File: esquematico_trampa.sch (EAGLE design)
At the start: 17 parts, among them U1 MICROCHIP_MCP3008-I-PMICROCHI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, U2 LM358PE3

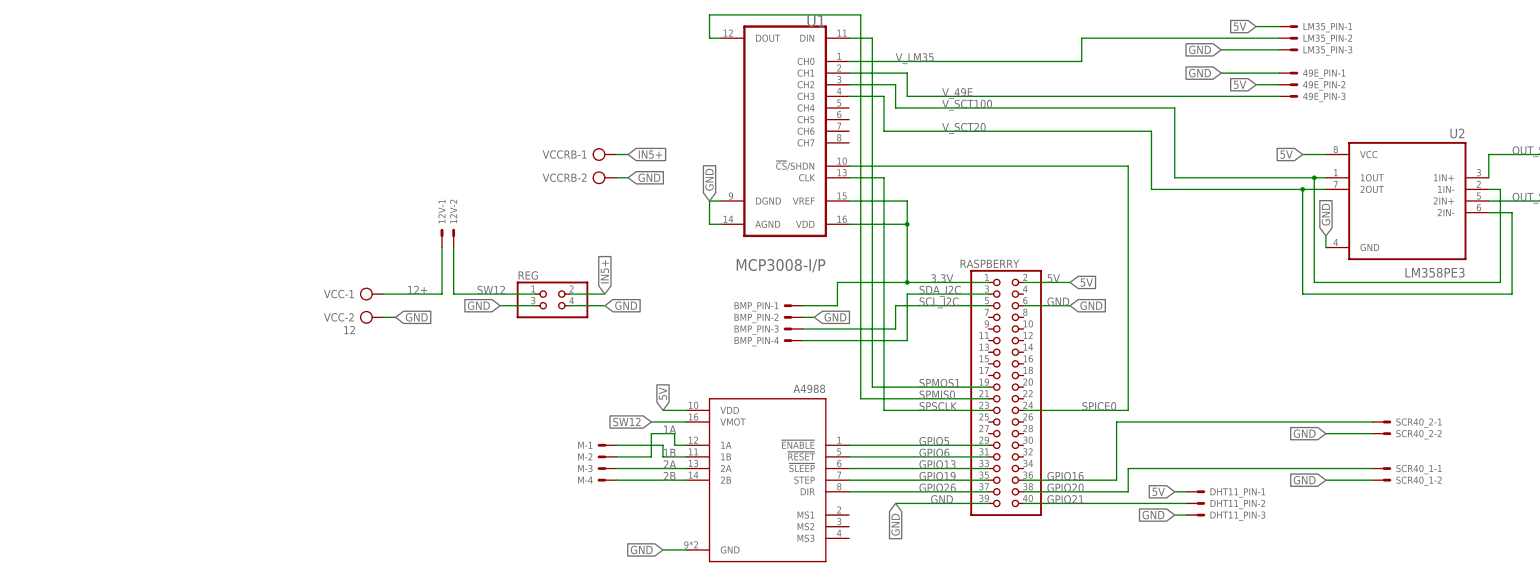
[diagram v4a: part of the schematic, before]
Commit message: esquematico con cambios en gpio7
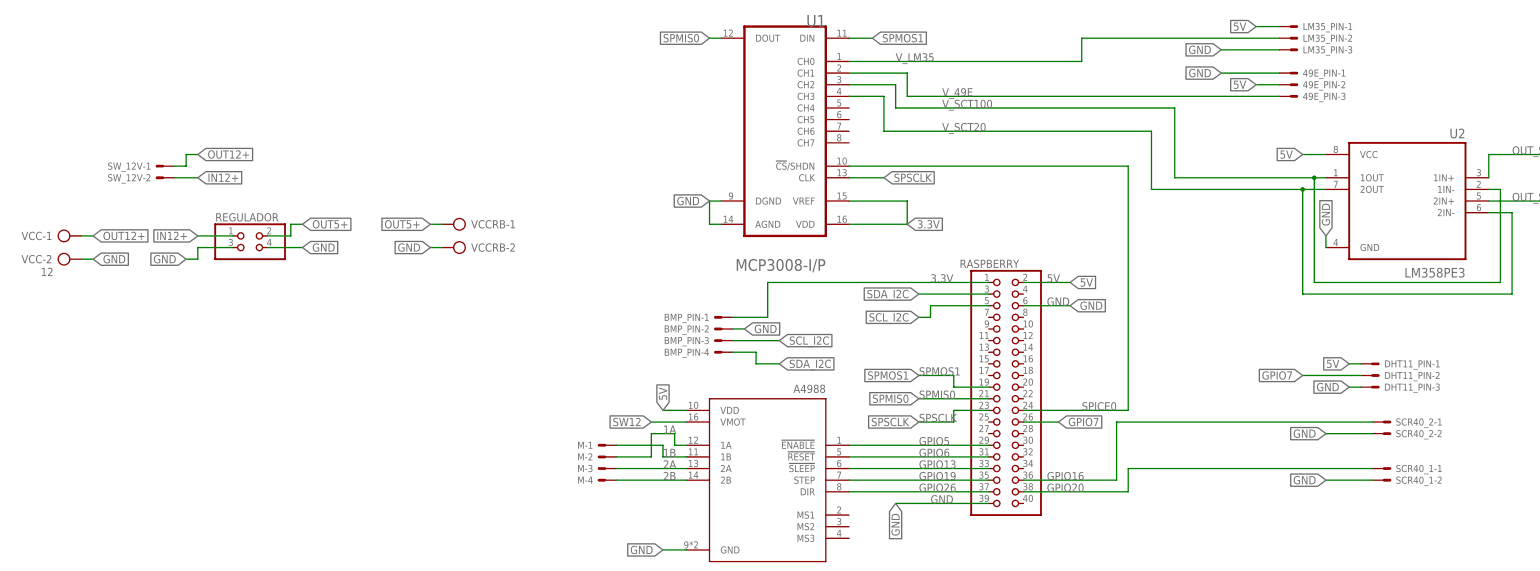
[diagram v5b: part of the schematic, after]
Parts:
- removed 12V: 22-23-2021, con-molex:22-23-2021
- removed REG: (no value), pinhead:PINHD-2X2
- added REGULADOR: (no value), pinhead:PINHD-2X2
- added SW_12V: 22-23-2021, con-molex:22-23-2021
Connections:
- removed net 12+: 12V-1.S, VCC-1.KL
- removed net GPIO21: DHT11_PIN-2.S, RASPBERRY.40
- removed net IN5+: REG.2, VCCRB-1.KL
- new net GPIO7: DHT11_PIN-2.S, RASPBERRY.26
- new net IN12+: REGULADOR.1, SW_12V-2.S
- new net OUT12+: SW_12V-1.S, VCC-1.KL
- new net OUT5+: REGULADOR.2, VCCRB-1.KL
- net GND: now also REGULADOR.3, REGULADOR.4; no longer REG.3, REG.4
- net SW12: no longer 12V-2.S, REG.1
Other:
- moved on the sheet: BMP_PIN-1, BMP_PIN-2, BMP_PIN-3, BMP_PIN-4, DHT11_PIN-1, DHT11_PIN-2, DHT11_PIN-3, VCC-1, VCC-2, VCCRB-1, VCCRB-2

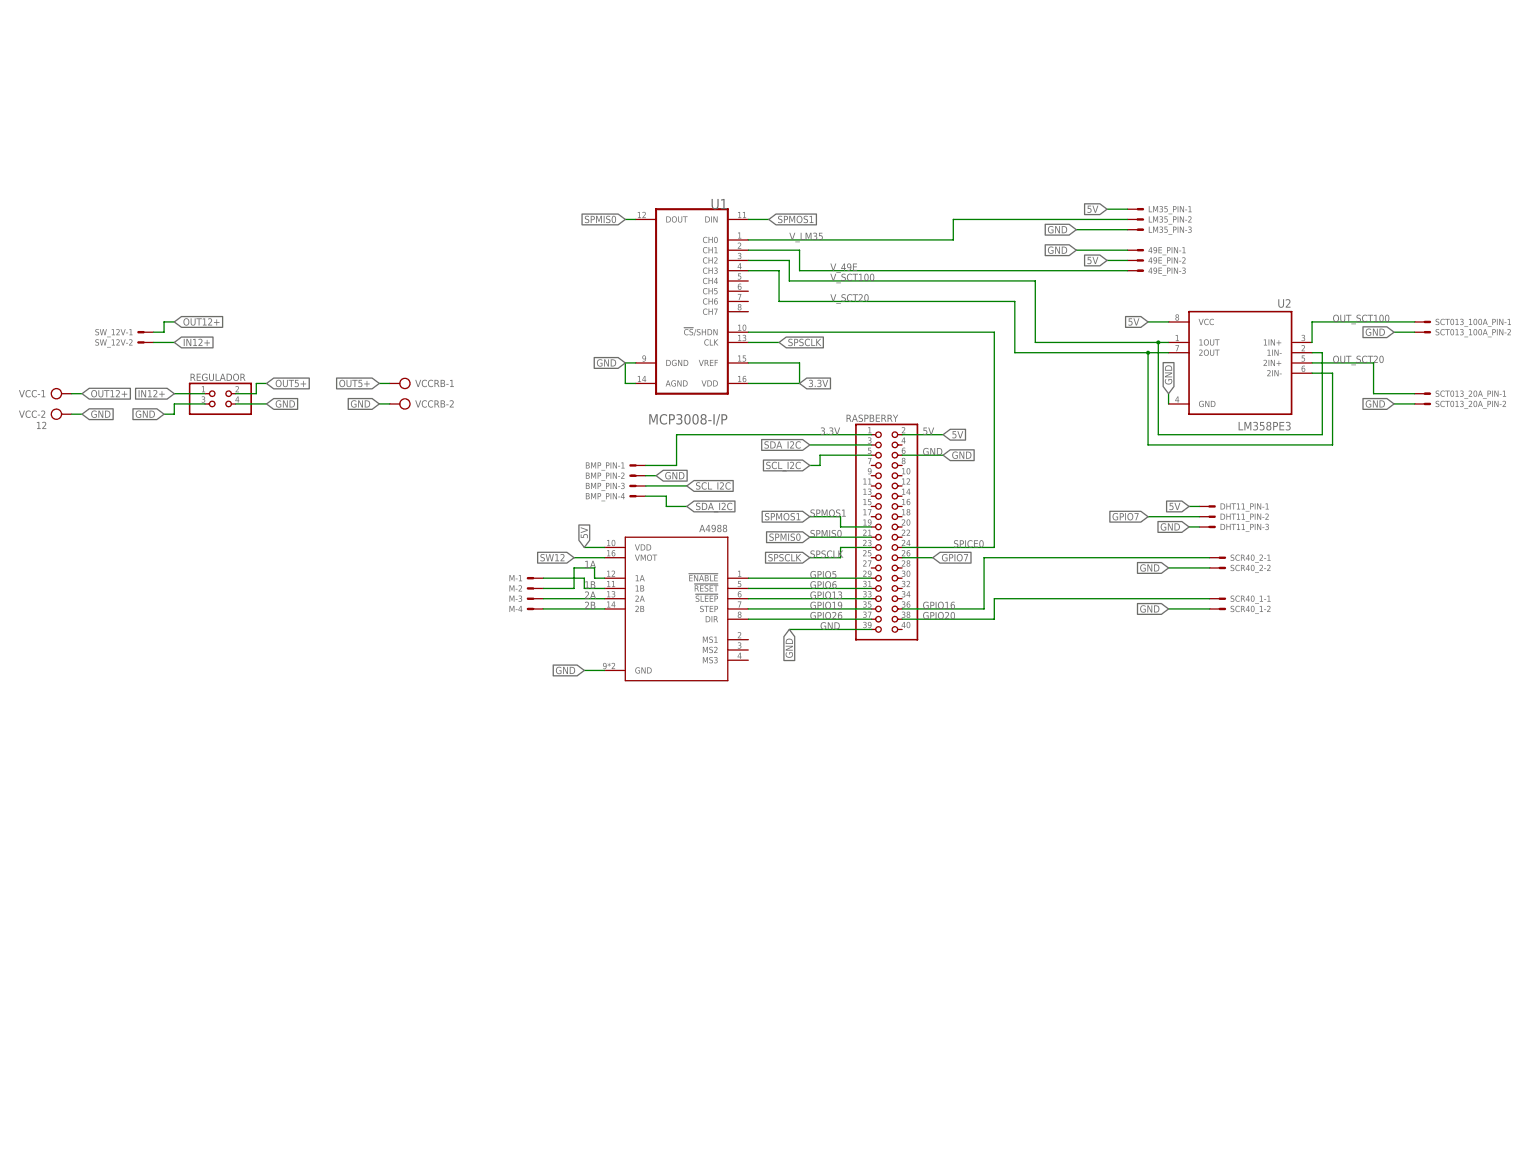
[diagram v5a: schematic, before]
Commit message: ordene todos los componentes
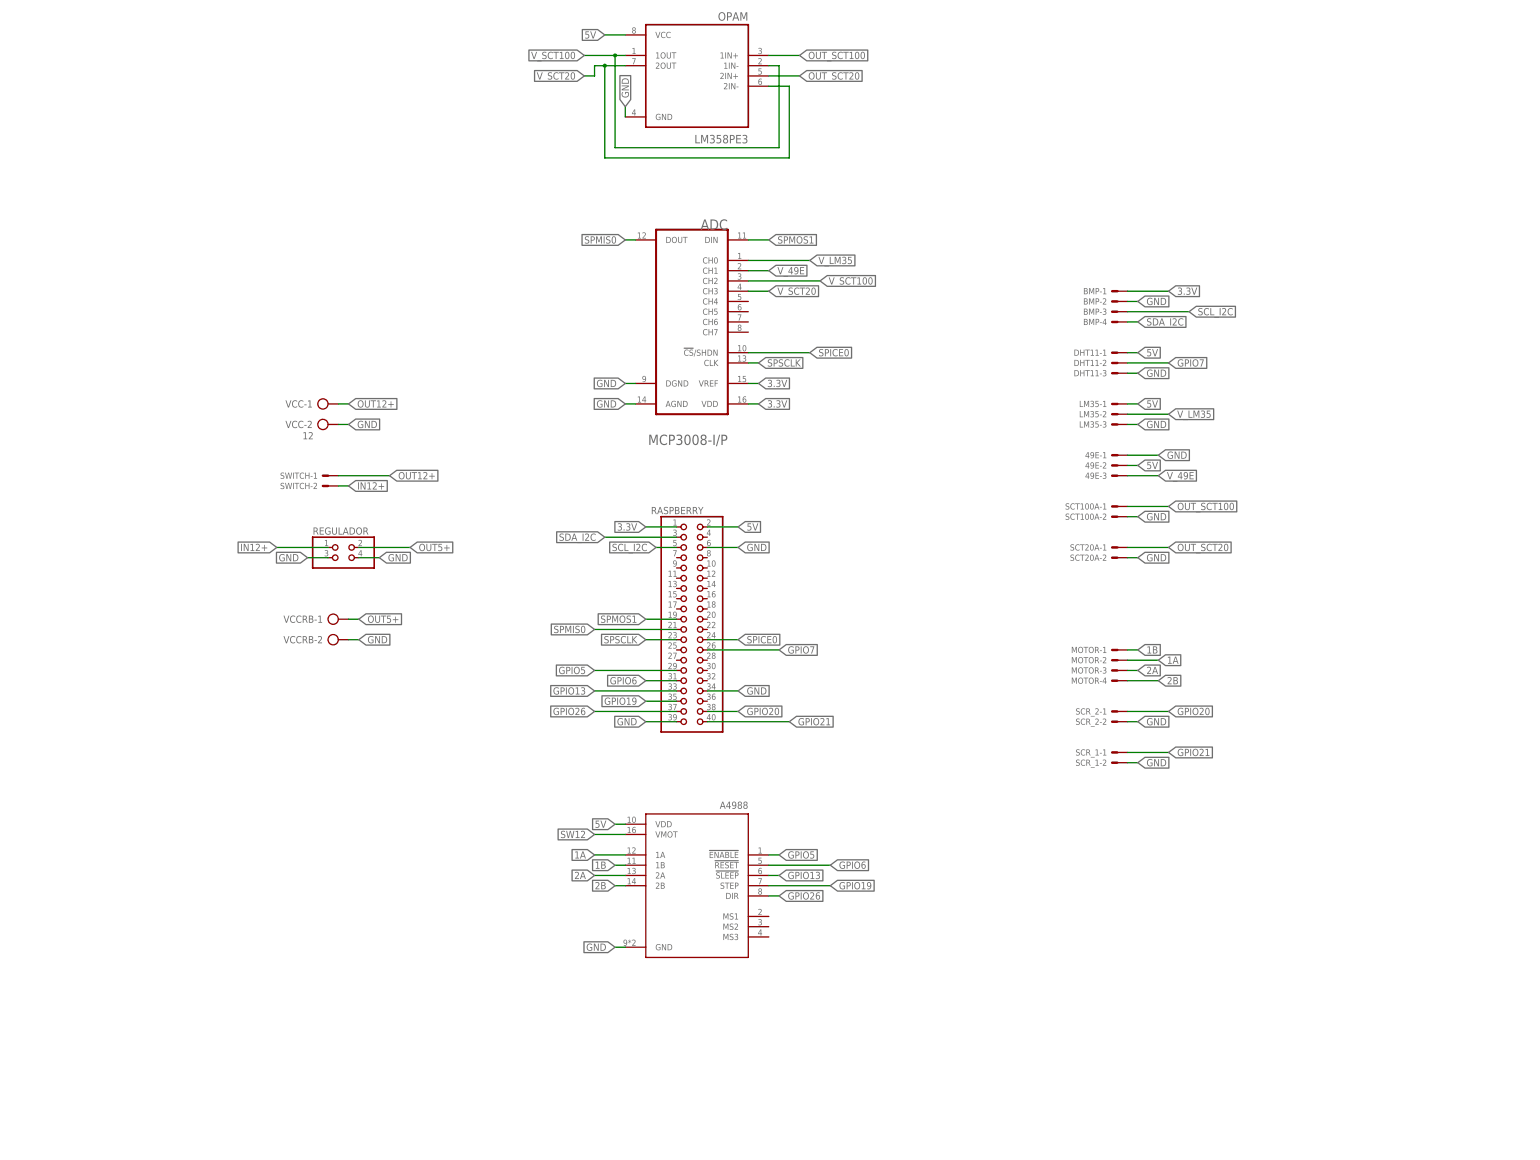
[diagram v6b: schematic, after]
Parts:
- removed 49E_PIN, DHT11_PIN, LM35_PIN: 22-23-2031, con-molex:22-23-2031
- removed BMP_PIN, M: 22-23-2041, con-molex:22-23-2041
- removed SCR40_1, SCR40_2, SCT013_100A_PIN, SCT013_20A_PIN, SW_12V: 22-23-2021, con-molex:22-23-2021
- removed U1: MICROCHIP_MCP3008-I-PMICROCHIP_MCP3008-I-P_0_0, P:MICROCHIP_MCP3008-I-PMICROCHIP_MCP3008-I-P_0_0
- removed U2: LM358PE3, LM358PE3:LM358PE3
- added 49E, DHT11, LM35: 22-23-2031, con-molex:22-23-2031
- added ADC: MICROCHIP_MCP3008-I-PMICROCHIP_MCP3008-I-P_0_0, P:MICROCHIP_MCP3008-I-PMICROCHIP_MCP3008-I-P_0_0
- added BMP, MOTOR: 22-23-2041, con-molex:22-23-2041
- added OPAM: LM358PE3, LM358PE3:LM358PE3
- added SCR_1, SCR_2, SCT100A, SCT20A, SWITCH: 22-23-2021, con-molex:22-23-2021
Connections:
- removed net GPIO16: RASPBERRY.36, SCR40_2-1.S
- new net GPIO21: RASPBERRY.40, SCR_1-1.S
- net 1A: now also MOTOR-2.S; no longer M-2.S
- net 1B: now also MOTOR-1.S; no longer M-1.S
- net 2A: now also MOTOR-3.S; no longer M-3.S
- net 2B: now also MOTOR-4.S; no longer M-4.S
- net 3.3V: now also ADC.VDD, ADC.VREF, BMP-1.S; no longer BMP_PIN-1.S, U1.VDD, U1.VREF
- net 5V: now also 49E-2.S, DHT11-1.S, LM35-1.S, OPAM.VCC; no longer 49E_PIN-2.S, DHT11_PIN-1.S, LM35_PIN-1.S, U2.VCC
- net GND: now also 49E-1.S, ADC.AGND, ADC.DGND, BMP-2.S, DHT11-3.S, LM35-3.S, OPAM.GND, RASPBERRY.34, SCR_1-2.S, SCR_2-2.S, SCT100A-2.S, SCT20A-2.S; no longer 49E_PIN-1.S, BMP_PIN-2.S, DHT11_PIN-3.S, LM35_PIN-3.S, SCR40_1-2.S, SCR40_2-2.S, SCT013_100A_PIN-2.S, SCT013_20A_PIN-2.S, U1.AGND, U1.DGND, U2.GND
- net GPIO20: now also SCR_2-1.S; no longer SCR40_1-1.S
- net GPIO7: now also DHT11-2.S; no longer DHT11_PIN-2.S
- net IN12+: now also SWITCH-2.S; no longer SW_12V-2.S
- net OUT12+: now also SWITCH-1.S; no longer SW_12V-1.S
- net OUT_SCT100: now also OPAM.1IN+, SCT100A-1.S; no longer SCT013_100A_PIN-1.S, U2.1IN+
- net OUT_SCT20: now also OPAM.2IN+, SCT20A-1.S; no longer SCT013_20A_PIN-1.S, U2.2IN+
- net SCL_I2C: now also BMP-3.S; no longer BMP_PIN-3.S
- net SDA_I2C: now also BMP-4.S; no longer BMP_PIN-4.S
- net SPICE0: now also ADC.!CS!/SHDN; no longer U1.!CS!/SHDN
- net SPMIS0: now also ADC.DOUT; no longer U1.DOUT
- net SPMOS1: now also ADC.DIN; no longer U1.DIN
- net SPSCLK: now also ADC.CLK; no longer U1.CLK
- net V_49E: now also 49E-3.S, ADC.CH1; no longer 49E_PIN-3.S, U1.CH1
- net V_LM35: now also ADC.CH0, LM35-2.S; no longer LM35_PIN-2.S, U1.CH0
- net V_SCT100: now also ADC.CH2, OPAM.1IN-, OPAM.1OUT; no longer U1.CH2, U2.1IN-, U2.1OUT
- net V_SCT20: now also ADC.CH3, OPAM.2IN-, OPAM.2OUT; no longer U1.CH3, U2.2IN-, U2.2OUT
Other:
- moved on the sheet: A4988, RASPBERRY, REGULADOR, VCC-1, VCC-2, VCCRB-1, VCCRB-2

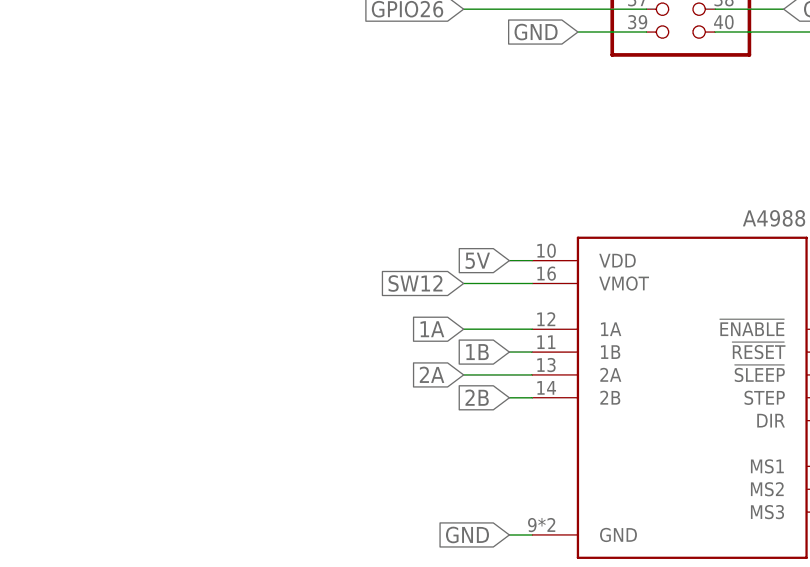
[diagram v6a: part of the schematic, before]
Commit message: conecte el vmotor a 12v
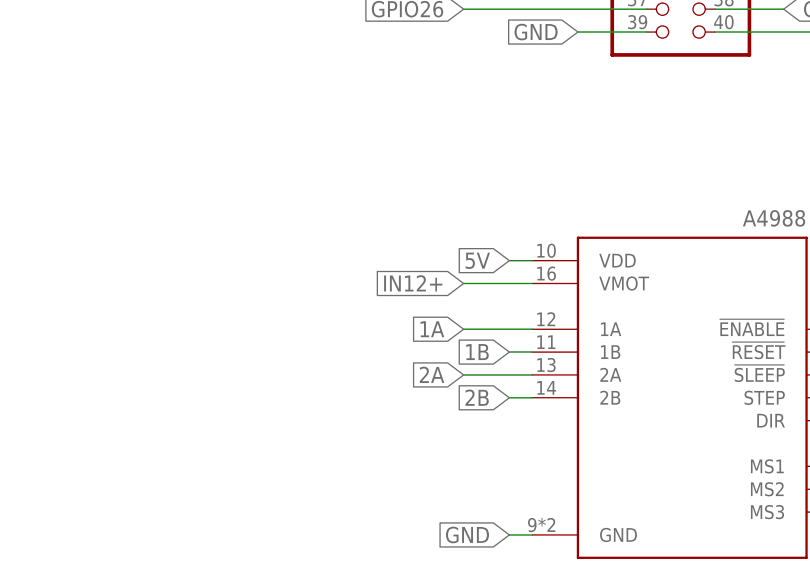
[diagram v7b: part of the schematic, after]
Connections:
- removed net SW12: A4988.VMOT
- net IN12+: now also A4988.VMOT
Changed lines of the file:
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@@
 <label x="-30.48" y="149.86" size="1.778" layer="95" xref="yes"/>
 </segment>
-</net>
-<net name="SW12" class="1">
 <segment>
 <pinref part="A4988" gate="G$1" pin="VMOT"/>

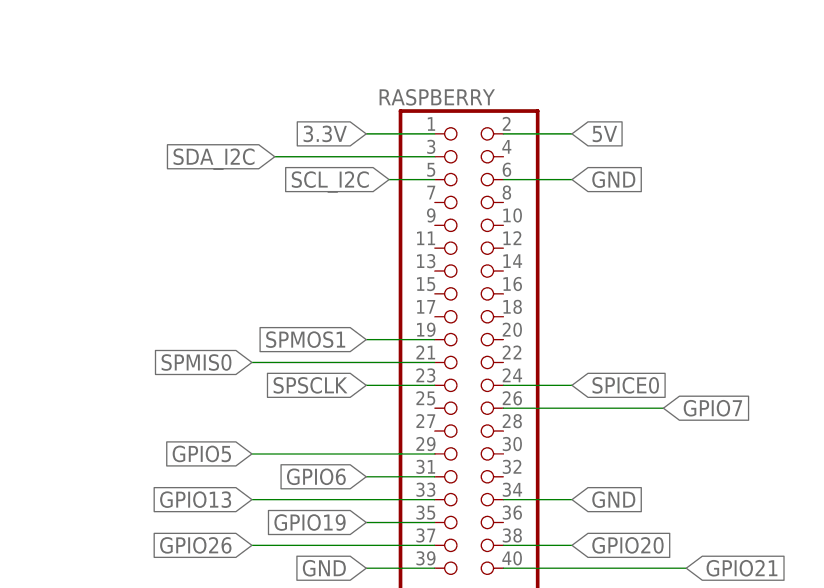
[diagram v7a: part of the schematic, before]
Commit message: esquematico ordenado y board 100 ruteado
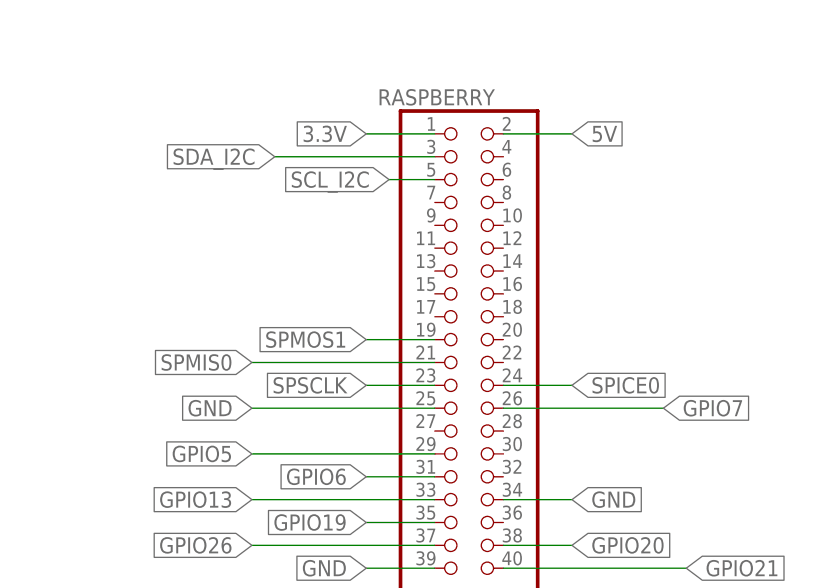
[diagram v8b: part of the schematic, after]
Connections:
- net GND: now also RASPBERRY.25; no longer RASPBERRY.6
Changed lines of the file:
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@@
-</segment>
-<segment>
-<pinref part="RASPBERRY" gate="A" pin="6"/>
-<wire x1="66.04" y1="134.62" x2="58.42" y2="134.62" width="0.1524" layer="91"/>
-<label x="66.04" y="134.62" size="1.778" layer="95" xref="yes"/>
 </segment>
 <segment>
@@
 <label x="66.04" y="99.06" size="1.778" layer="95" xref="yes"/>
 </segment>
+<segment>
+<pinref part="RASPBERRY" gate="A" pin="25"/>
+<wire x1="50.8" y1="109.22" x2="30.48" y2="109.22" width="0.1524" layer="91"/>
+<label x="30.48" y="109.22" size="1.778" layer="95" rot="R180" xref="yes"/>
+</segment>
 </net>
